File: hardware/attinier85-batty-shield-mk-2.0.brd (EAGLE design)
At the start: 36 x 25 mm, 6 parts, among them U1 ATTINIEST85_SHIELDV2

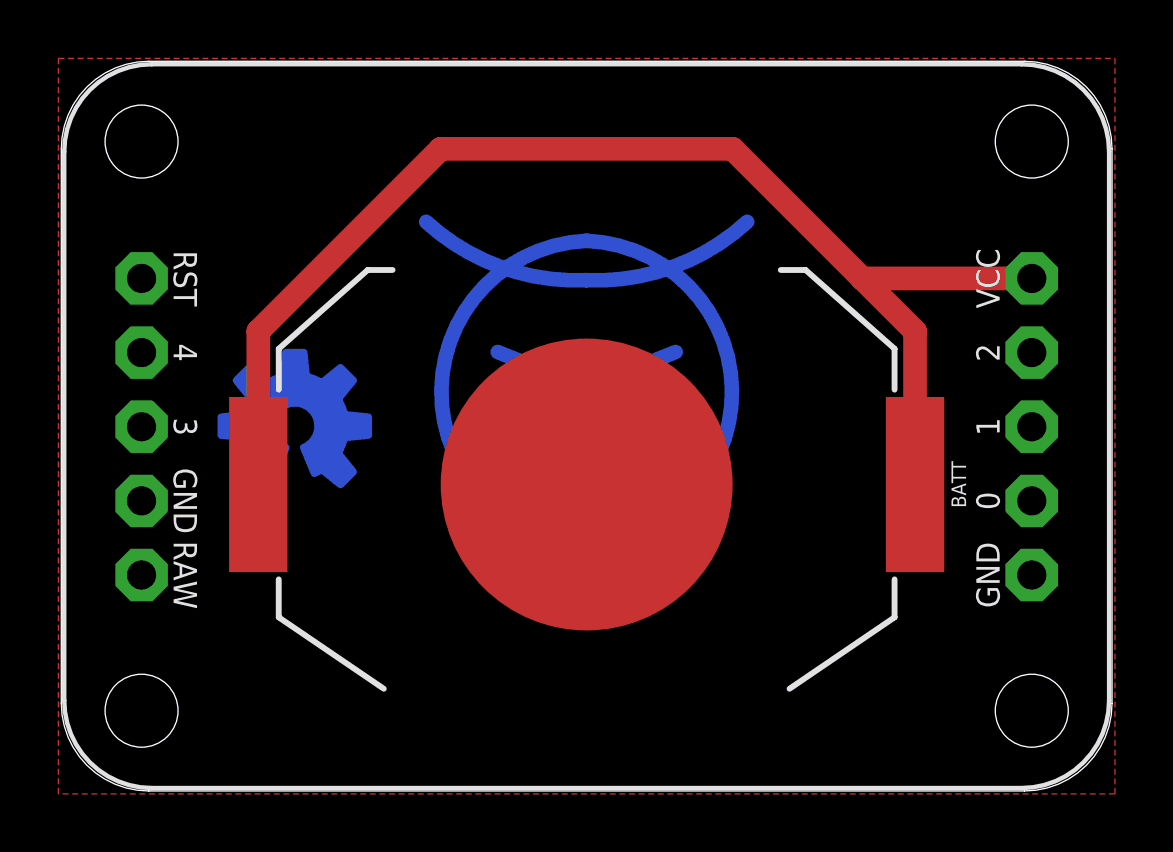
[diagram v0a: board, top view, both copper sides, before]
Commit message: renaming parts
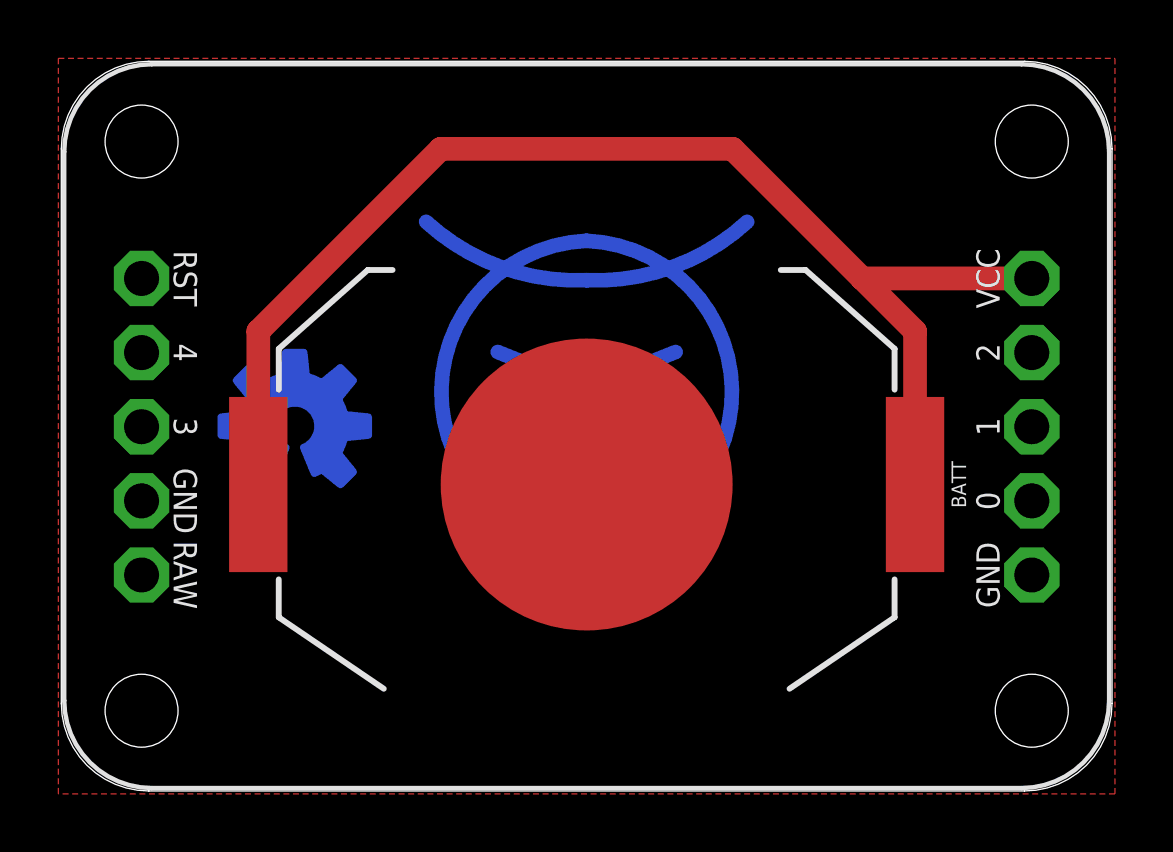
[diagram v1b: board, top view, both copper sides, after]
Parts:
- U1: value ATTINIEST85_SHIELDV2 -> ATTINIER85_SHIELDV2; device A_butts:ATTINIEST85_SHIELD_V2 -> A_butts:ATTINIER85_SHIELD_V2
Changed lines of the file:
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@@
 <attribute name="DESIGNER" value="Nobody" x="13.97" y="-1.27" size="1.778" layer="27" display="off"/>
 </element>
-<element name="U1" library="A_butts" package="ATTINIEST85_SHIELD_V2" value="ATTINIEST85_SHIELDV2" x="18" y="12.5"/>
+<element name="U1" library="A_butts" package="ATTINIER85_SHIELD_V2" value="ATTINIER85_SHIELDV2" x="18" y="12.5"/>
 <element name="BATT" library="A_butts" package="BATTCON_20MM_MINE" value="CR2032" x="18" y="10.5" rot="R270"/>
 <element name="U$3" library="A_butts" package="CC-BY-SA-4.0-NO-URL" value="" x="28" y="12.5" rot="MR0"/>
